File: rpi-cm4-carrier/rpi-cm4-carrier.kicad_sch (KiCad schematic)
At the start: 0 parts

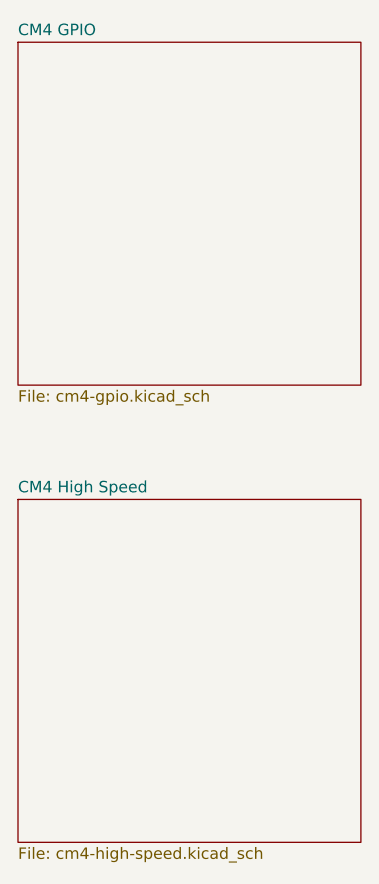
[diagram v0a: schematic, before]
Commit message: Wired Ethernet data
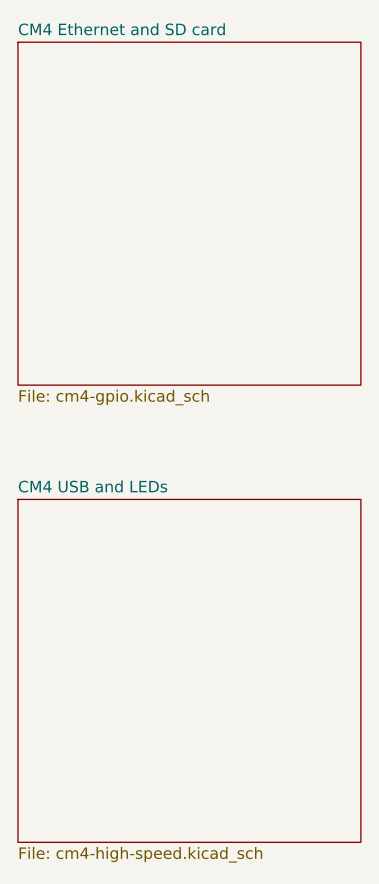
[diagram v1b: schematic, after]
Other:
- sheet CM4 GPIO renamed CM4 Ethernet and SD card
- sheet CM4 High Speed renamed CM4 USB and LEDs
